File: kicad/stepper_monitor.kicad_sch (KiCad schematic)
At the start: 90 parts, among them J1 Conn_01x02_Pin, J2 Conn_01x04_Pin, J3 USB_C_Receptacle_USB2.0, J4 Conn_01x04_Pin, J5 Conn_01x04_Pin, J6 JTAG, M1 Motor-simple_stepper_motor_an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, Q1 MMDT2222A, SW1 SW_Push, U1 5V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

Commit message: Used ESP32 with Integrated antenna
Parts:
- U3: footprint stepper_monitor:ESP32-WROOM-32UE -> stepper_monitor:ESP32-WROOM-32E
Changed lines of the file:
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@@
       (effects (font (size 1.27 1.27)))
     )
-    (property "Footprint" "stepper_monitor:ESP32-WROOM-32UE" (at 240.03 22.606 0)
+    (property "Footprint" "stepper_monitor:ESP32-WROOM-32E" (at 240.03 22.606 0)
       (effects (font (size 1.27 1.27)) hide)
     )

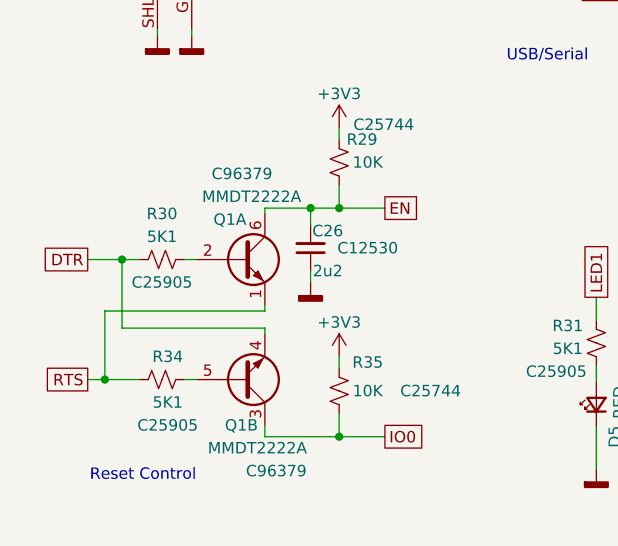
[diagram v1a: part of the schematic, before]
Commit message: Replaced Extended part transistors with basic mosfets
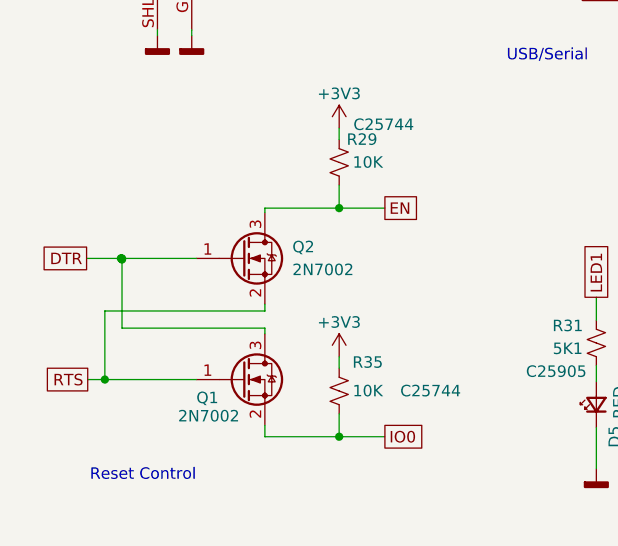
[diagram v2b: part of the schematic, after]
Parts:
- removed C26: 2u2, Capacitor_SMD:C_0402_1005Metric, symbol Device:C_Small
- removed Q1: MMDT2222A, stepper_monitor:SOT-363_SC-70-6, symbol Transistor_BJT:MMDT2222A
- removed R30, R34: 5K1, Resistor_SMD:R_0402_1005Metric, symbol Device:R_Small_US
- added Q1, Q2: 2N7002, Package_TO_SOT_SMD:SOT-23, symbol Transistor_FET:2N7002
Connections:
- net DTR: now also Q1.3 (D), Q2.1 (G)
- net EN: now also Q2.3 (D)
- net IO0: now also Q1.2 (S)
- net RTS: now also Q1.1 (G), Q2.2 (S)

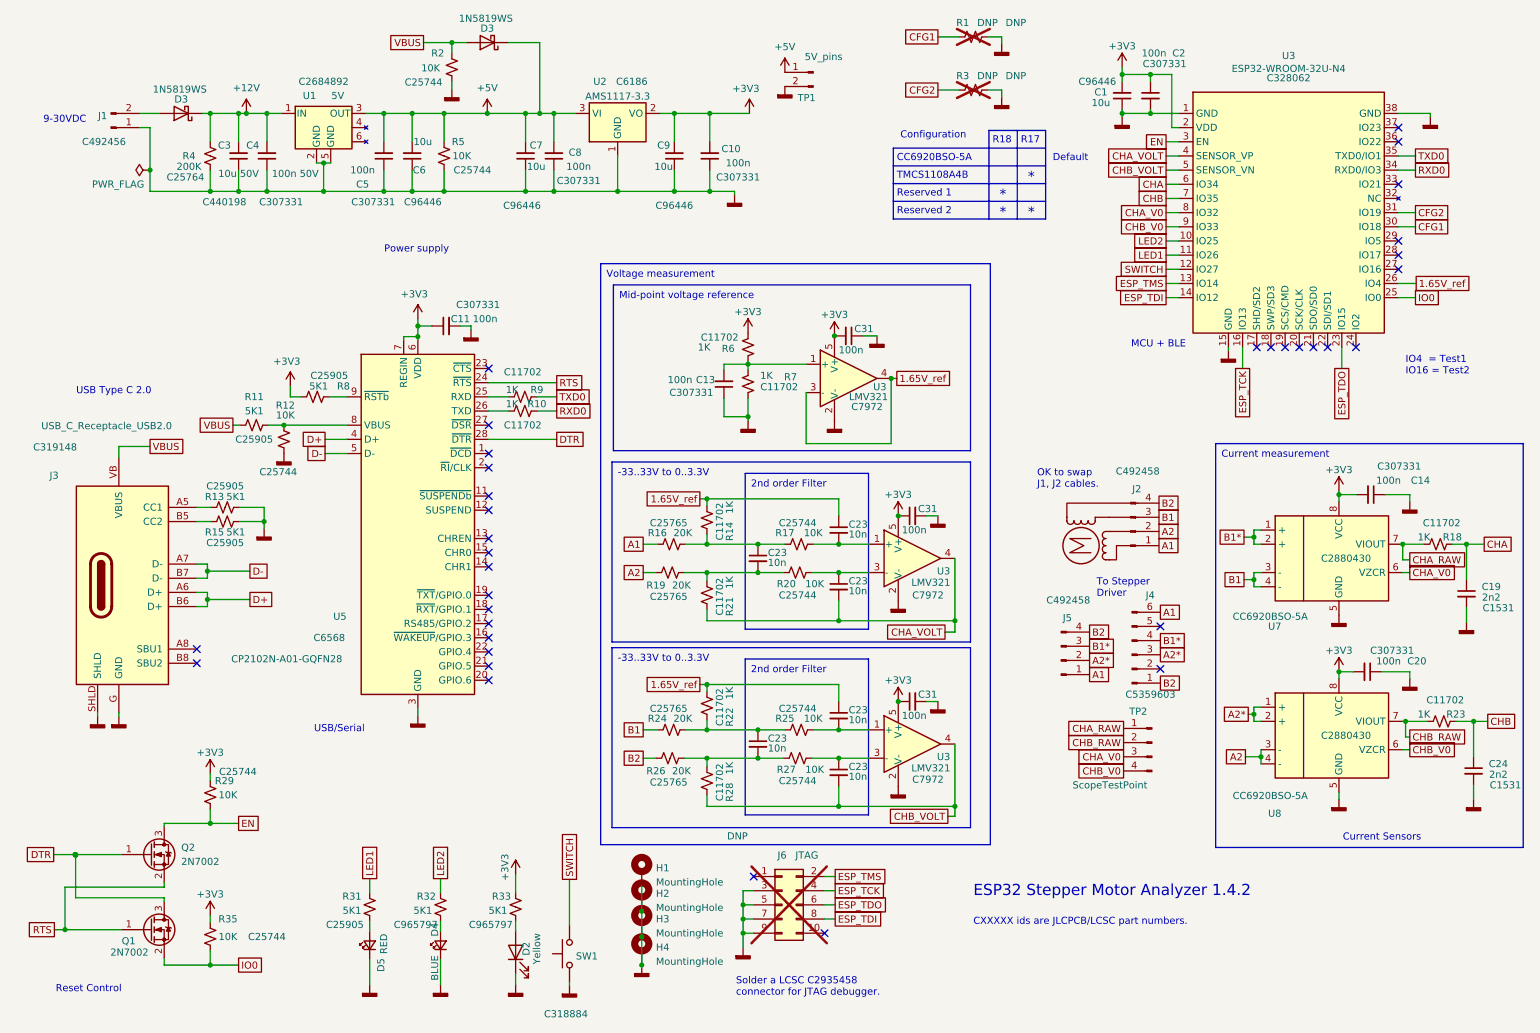
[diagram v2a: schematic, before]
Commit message: Added 5pin uart programming header. Fixed led resistor part number.  Normal switching reverse polarity diode
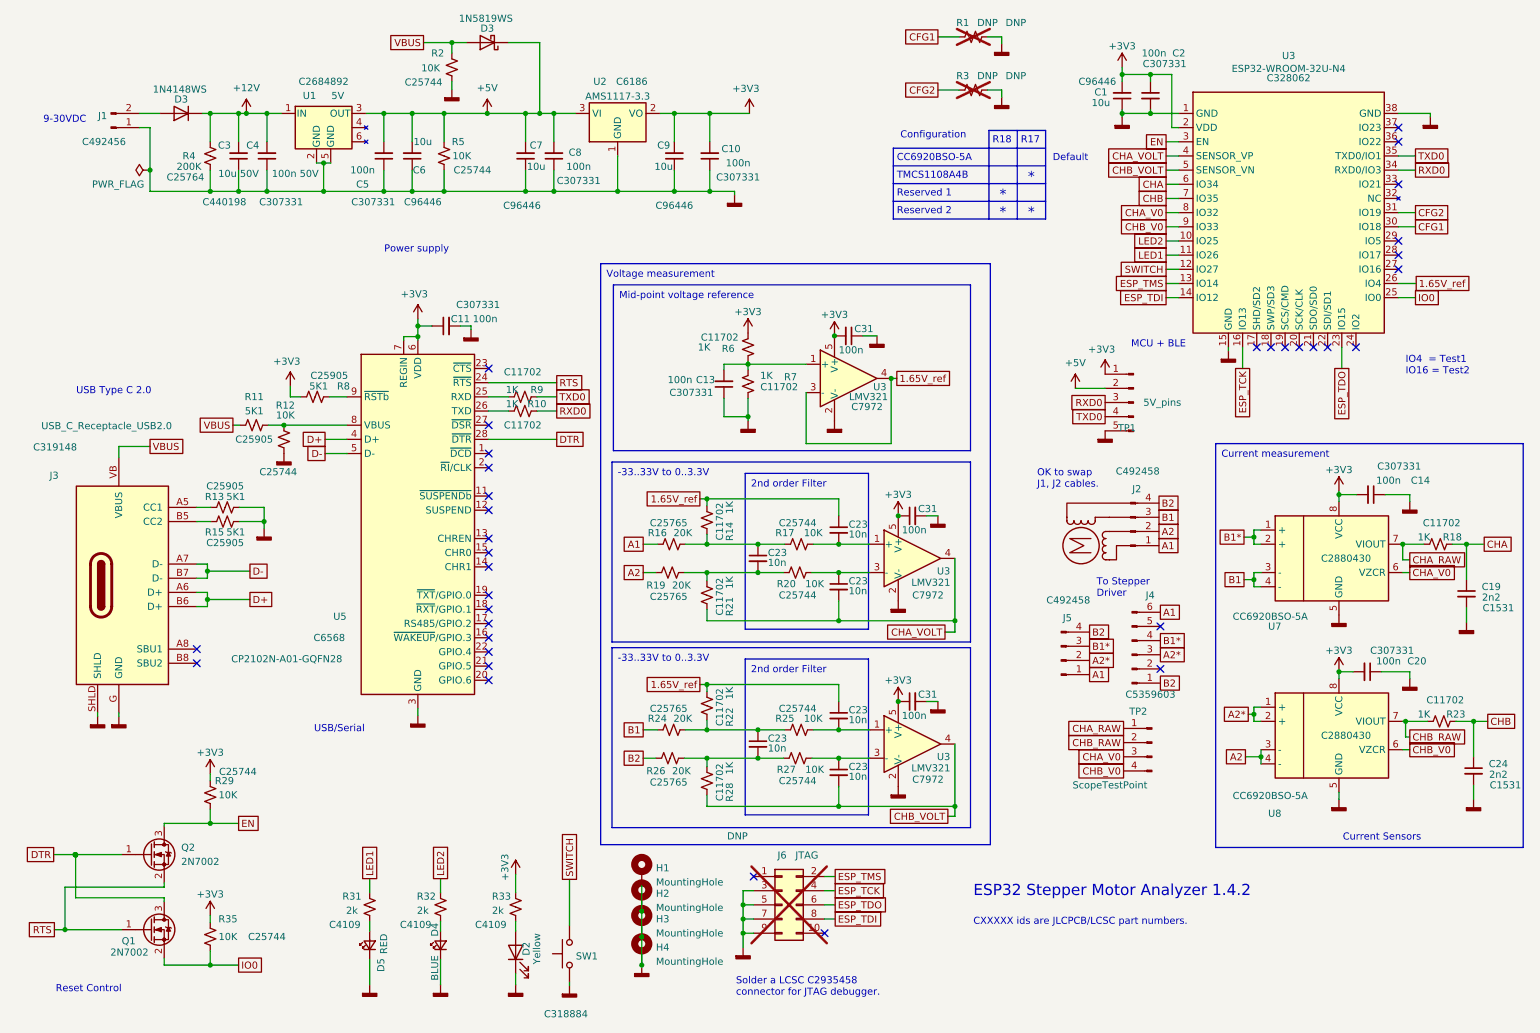
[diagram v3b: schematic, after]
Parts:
- D3: value 1N5819WS -> 1N4148WS; symbol Diode:1N5819 -> Diode:1N4148WS; LCSC C191023 -> C2128
- R31: value 5K1 -> 2k; LCSC C25905 -> C4109
- R32, R33: value 5K1 -> 2k; LCSC C965797 -> C4109
- TP1: footprint Connector_PinHeader_2.54mm:PinHeader_1x02_P2.54mm_Vertical -> Connector_PinHeader_2.54mm:PinHeader_1x05_P2.54mm_Vertical; symbol Connector:Conn_01x02_Pin -> Connector:Conn_01x05_Pin
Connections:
- net +3V3: now also TP1.1 (Pin_1)
- net +5V: now also TP1.2 (Pin_2); no longer TP1.1 (Pin_1)
- net GNDD: now also TP1.5 (Pin_5); no longer TP1.2 (Pin_2)
- net RXD0: now also TP1.3 (Pin_3)
- net TXD0: now also TP1.4 (Pin_4)
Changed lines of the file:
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@@
     (stroke (width 0) (type default))
   )
+  (wire (pts (xy 202.438 82.042) (xy 207.772 82.042))
+    (stroke (width 0) (type default))
+  )
   (wire (pts (xy 47.371 42.926) (xy 47.371 46.736))
     (stroke (width 0) (type default))
@@
     )
   )
+  (global_label "TXD0" (shape passive) (at 207.772 87.122 180) (fields_autoplaced)
+    (effects (font (size 1.27 1.27)) (justify right))
+    (property "Intersheetrefs" "${INTERSHEET_REFS}" (at 201.8163 87.122 0)
+      (effects (font (size 1.27 1.27)) (justify right) hide)
+    )
+  )
   (global_label "A2" (shape passive) (at 124.968 115.062 180) (fields_autoplaced)
     (effects (font (size 1.27 1.27)) (justify right))
@@
     )
   )
+  (global_label "RXD0" (shape passive) (at 207.772 84.582 180) (fields_autoplaced)
+    (effects (font (size 1.27 1.27)) (justify right))
+    (property "Intersheetrefs" "${INTERSHEET_REFS}" (at 201.5139 84.582 0)
+      (effects (font (size 1.27 1.27)) (justify right) hide)
+    )
+  )
   (global_label "CHB_VOLT" (shape passive) (at 218.694 42.926 180) (fields_autoplaced)
     (effects (font (size 1.27 1.27)) (justify right))
@@
       (effects (font (size 1.27 1.27)))
     )
-    (property "Value" "5K1" (at 72.771 175.641 0)
+    (property "Value" "2k" (at 72.771 175.641 0)
       (effects (font (size 1.27 1.27)))
     )
@@
       (effects (font (size 1.27 1.27)) hide)
     )
-    (property "LCSC" "C25905" (at 71.501 178.181 0)
+    (property "LCSC" "C4109" (at 71.501 178.181 0)
       (effects (font (size 1.27 1.27)))
     )
@@
       (effects (font (size 1.27 1.27)))
     )
-    (property "Value" "5K1" (at 85.471 175.641 0)
+    (property "Value" "2k" (at 85.471 175.641 0)
       (effects (font (size 1.27 1.27)))
     )
@@
       (effects (font (size 1.27 1.27)) hide)
     )
-    (property "LCSC" "C965797" (at 84.201 178.181 0)
+    (property "LCSC" "C4109" (at 84.201 178.181 0)
       (effects (font (size 1.27 1.27)))
     )
@@
     )
   )
-  (symbol (lib_id "power:+5V") (at 150.368 25.4 0) (unit 1)
+  (symbol (lib_id "power:+5V") (at 202.438 82.042 0) (unit 1)
     (in_bom yes) (on_board yes) (dnp no) (fields_autoplaced)
-    (property "Reference" "#PWR03" (at 150.368 29.21 0)
+    (property "Reference" "#PWR03" (at 202.438 85.852 0)
       (effects (font (size 1.27 1.27)) hide)
     )
-    (property "Value" "+5V" (at 150.368 20.828 0)
+    (property "Value" "+5V" (at 202.438 77.47 0)
       (effects (font (size 1.27 1.27)))
     )
-    (property "Footprint" "" (at 150.368 25.4 0)
+    (property "Footprint" "" (at 202.438 82.042 0)
       (effects (font (size 1.27 1.27)) hide)
     )
-    (property "Datasheet" "" (at 150.368 25.4 0)
+    (property "Datasheet" "" (at 202.438 82.042 0)
       (effects (font (size 1.27 1.27)) hide)
     )
@@
     )
   )
-  (symbol (lib_id "power:GNDD") (at 150.368 27.94 0) (unit 1)
+  (symbol (lib_id "power:GNDD") (at 207.772 89.662 0) (unit 1)
     (in_bom yes) (on_board yes) (dnp no)
-    (property "Reference" "#PWR04" (at 150.368 34.29 0)
+    (property "Reference" "#PWR04" (at 207.772 96.012 0)
       (effects (font (size 1.27 1.27)) hide)
     )
-    (property "Value" "GNDD" (at 150.4696 31.877 0)
+    (property "Value" "GNDD" (at 207.8736 93.599 0)
       (effects (font (size 1.27 1.27)) hide)
     )
-    (property "Footprint" "" (at 150.368 27.94 0)
+    (property "Footprint" "" (at 207.772 89.662 0)
       (effects (font (size 1.27 1.27)) hide)
     )
-    (property "Datasheet" "" (at 150.368 27.94 0)
+    (property "Datasheet" "" (at 207.772 89.662 0)
       (effects (font (size 1.27 1.27)) hide)
     )
@@
     )
   )
+  (symbol (lib_id "power:+3V3") (at 207.772 79.502 0) (unit 1)
+    (in_bom yes) (on_board yes) (dnp no)
+    (property "Reference" "#PWR042" (at 207.772 83.312 0)
+      (effects (font (size 1.27 1.27)) hide)
+    )
+    (property "Value" "+3V3" (at 207.137 75.057 0)
+      (effects (font (size 1.27 1.27)))
+    )
+    (property "Footprint" "" (at 207.772 79.502 0)
+      (effects (font (size 1.27 1.27)) hide)
+    )
+    (property "Datasheet" "" (at 207.772 79.502 0)
+      (effects (font (size 1.27 1.27)) hide)
+    )
+    (pin "1")
+    (instances
+      (project "stepper_monitor"
+        (path "/ab9a1617-734a-47a3-94aa-b13da0ec18df"
+          (reference "#PWR042") (unit 1)
+        )
+      )
+    )
+  )
   (symbol (lib_id "power:GNDD") (at 272.542 123.952 0) (unit 1)
     (in_bom yes) (on_board yes) (dnp no)
@@
     )
   )
-  (symbol (lib_id "Connector:Conn_01x02_Pin") (at 155.448 25.4 0) (mirror y) (unit 1)
+  (symbol (lib_id "Connector:Conn_01x05_Pin") (at 212.852 84.582 0) (mirror y) (unit 1)
     (in_bom yes) (on_board yes) (dnp no)
-    (property "Reference" "TP1" (at 152.654 29.972 0)
+    (property "Reference" "TP1" (at 210.058 89.154 0)
       (effects (font (size 1.27 1.27)) (justify right))
     )
-    (property "Value" "5V_pins" (at 153.924 22.606 0)
+    (property "Value" "5V_pins" (at 214.63 84.582 0)
       (effects (font (size 1.27 1.27)) (justify right))
     )
-    (property "Footprint" "Connector_PinHeader_2.54mm:PinHeader_1x02_P2.54mm_Vertical" (at 155.448 25.4 0)
+    (property "Footprint" "Connector_PinHeader_2.54mm:PinHeader_1x05_P2.54mm_Vertical" (at 212.852 84.582 0)
       (effects (font (size 1.27 1.27)) hide)
     )
-    (property "Datasheet" "~" (at 155.448 25.4 0)
+    (property "Datasheet" "~" (at 212.852 84.582 0)
       (effects (font (size 1.27 1.27)) hide)
     )
-    (property "LCSC" "" (at 154.178 36.195 0)
+    (property "LCSC" "" (at 211.582 95.377 0)
       (effects (font (size 1.27 1.27)))
     )
     (pin "1")
     (pin "2")
+    (pin "3")
+    (pin "4")
+    (pin "5")
     (instances
       (project "stepper_monitor"
@@
       (effects (font (size 1.27 1.27)))
     )
-    (property "Value" "5K1" (at 98.933 175.641 0)
+    (property "Value" "2k" (at 98.933 175.641 0)
       (effects (font (size 1.27 1.27)))
     )
@@
       (effects (font (size 1.27 1.27)) hide)
     )
-    (property "LCSC" "C965797" (at 97.663 178.181 0)
+    (property "LCSC" "C4109" (at 97.663 178.181 0)
       (effects (font (size 1.27 1.27)))
     )
@@
     )
   )
-  (symbol (lib_id "Diode:1N5819") (at 42.164 32.766 180) (unit 1)
+  (symbol (lib_id "Diode:1N4148WS") (at 42.164 32.766 180) (unit 1)
     (in_bom yes) (on_board yes) (dnp no)
     (property "Reference" "D3" (at 42.164 30.226 0)
       (effects (font (size 1.27 1.27)))
     )
-    (property "Value" "1N5819WS" (at 41.91 28.448 0)
+    (property "Value" "1N4148WS" (at 41.91 28.448 0)
       (effects (font (size 1.27 1.27)))
     )
@@
       (effects (font (size 1.27 1.27)) hide)
     )
-    (property "Datasheet" "https://datasheet.lcsc.com/lcsc/2204281430_Guangdong-Hottech-1N5819WS_C191023.pdf" (at 42.164 32.766 0)
+    (property "Datasheet" "https://www.vishay.com/docs/85751/1n4148ws.pdf" (at 42.164 32.766 0)
+      (effects (font (size 1.27 1.27)) hide)
+    )
+    (property "LCSC" "C2128" (at 42.4815 25.781 0)
+      (effects (font (size 1.27 1.27)) hide)
+    )
+    (property "Sim.Device" "D" (at 42.164 32.766 0)
       (effects (font (size 1.27 1.27)) hide)
     )
-    (property "LCSC" "C191023" (at 42.4815 25.781 0)
+    (property "Sim.Pins" "1=K 2=A" (at 42.164 32.766 0)
       (effects (font (size 1.27 1.27)) hide)
     )
